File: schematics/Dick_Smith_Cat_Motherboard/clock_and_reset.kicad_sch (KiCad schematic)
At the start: 23 parts, among them Q1 9018, Q52 9018, U1 NE555, U17 74LS86, U19 74LS125, U21 74LS161, U31 74LS74, U34 74LS08, U36 74LS04, U4 74LS04

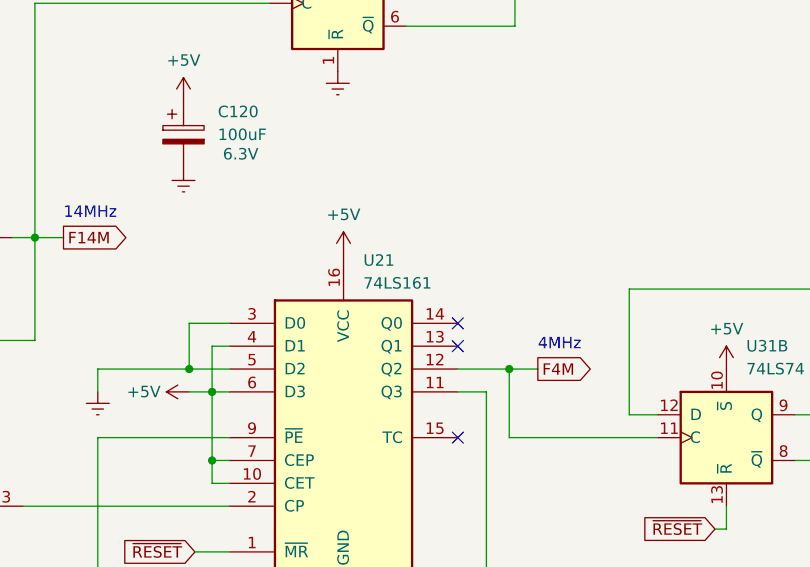
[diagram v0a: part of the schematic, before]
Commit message: Fix chip numbers in the motherboard schematic
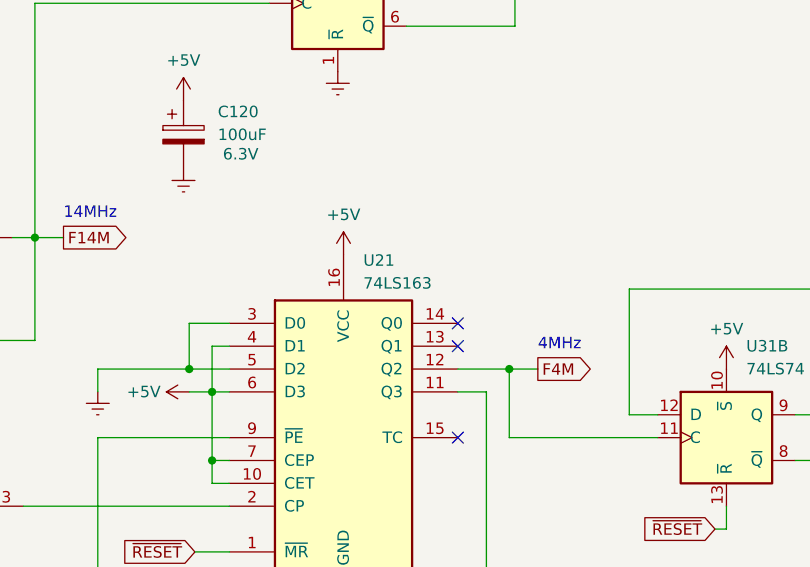
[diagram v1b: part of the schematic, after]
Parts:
- removed U21: 74LS161, Package_DIP:DIP-16_W7.62mm, symbol 74xx:74LS161
- added U21: 74LS163, Package_DIP:DIP-16_W7.62mm, symbol 74xx:74LS163
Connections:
- net +5V: now also U21.10 (CET), U21.16 (VCC), U21.4 (D1), U21.6 (D3), U21.7 (CEP)
- net Earth: now also U21.3 (D0), U21.5 (D2), U21.8 (GND)
- net F4M: now also U21.12 (Q2)
- net ~{RESET}: now also U21.1 (~{MR})
- net at U17.3: now also U21.2 (CP)
- new net: U21.11 (Q3), U21.9 (~{PE})
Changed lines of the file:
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@@
+    )
+  )
+  (symbol (lib_id "74xx:74LS163") (at 173.99 92.71 0) (unit 1)
+    (in_bom yes) (on_board yes) (dnp no) (fields_autoplaced)
+    (property "Reference" "U21" (at 176.1841 73.025 0)
+      (effects (font (size 1.27 1.27)) (justify left))
+    )
+    (property "Value" "74LS163" (at 176.1841 75.565 0)
+      (effects (font (size 1.27 1.27)) (justify left))
+    )
+    (property "Footprint" "Package_DIP:DIP-16_W7.62mm" (at 173.99 92.71 0)
+      (effects (font (size 1.27 1.27)) hide)
+    )
+    (property "Datasheet" "http://www.ti.com/lit/gpn/sn74LS163" (at 173.99 92.71 0)
+      (effects (font (size 1.27 1.27)) hide)
+    )
+    (pin "6")
+    (pin "4")
+    (pin "2")
+    (pin "7")
+    (pin "3")
+    (pin "8")
+    (pin "12")
+    (pin "14")
+    (pin "11")
+    (pin "13")
+    (pin "9")
+    (pin "15")
+    (pin "5")
+    (pin "1")
+    (pin "10")
+    (pin "16")
+    (instances
+      (project "Dick_Smith_Cat_Motherboard"
+        (path "/b825002a-fcdd-4970-89c6-1645cf48180b/51b7fb88-92ae-4aa8-81bc-d933ff6e242f"
+          (reference "U21") (unit 1)
+        )
+      )
     )
   )
@@
         )
       )
-    )
-  )
-  (symbol (lib_id "74xx:74LS161") (at 173.99 92.71 0) (unit 1)
-    (in_bom yes) (on_board yes) (dnp no) (fields_autoplaced)
-    (property "Reference" "U21" (at 176.1841 73.025 0)
-      (effects (font (size 1.27 1.27)) (justify left))
-    )
-    (property "Value" "74LS161" (at 176.1841 75.565 0)
-      (effects (font (size 1.27 1.27)) (justify left))
-    )
-    (property "Footprint" "Package_DIP:DIP-16_W7.62mm" (at 173.99 92.71 0)
-      (effects (font (size 1.27 1.27)) hide)
-    )
-    (property "Datasheet" "http://www.ti.com/lit/gpn/sn74LS161" (at 173.99 92.71 0)
-      (effects (font (size 1.27 1.27)) hide)
-    )
-    (pin "2")
-    (pin "5")
-    (pin "6")
-    (pin "7")
-    (pin "11")
-    (pin "1")
-    (pin "13")
-    (pin "12")
-    (pin "10")
-    (pin "8")
-    (pin "16")
-    (pin "9")
-    (pin "3")
-    (pin "15")
-    (pin "4")
-    (pin "14")
-    (instances
-      (project "Dick_Smith_Cat_Motherboard"
-        (path "/b825002a-fcdd-4970-89c6-1645cf48180b/51b7fb88-92ae-4aa8-81bc-d933ff6e242f"
-          (reference "U21") (unit 1)
-        )
-      )
